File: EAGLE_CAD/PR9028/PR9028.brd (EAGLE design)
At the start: 65.9 x 66 mm, 61 parts, among them SW1 C&K_PTS645, T1 TPTP20R, T10 TPTP20R, T11 TPTP20R, T12 TPTP20R, T13 TPTP20R, T14 TPTP20R, T15 TPTP20R, T16 TPTP20R, T17 TPTP20R, T2 TPTP20R, T4 TPTP20R, T5 TPTP20R, T6 TPTP20R, T7 TPTP20R, T8 TPTP20R, T9 TPTP20R, U1 FMIC

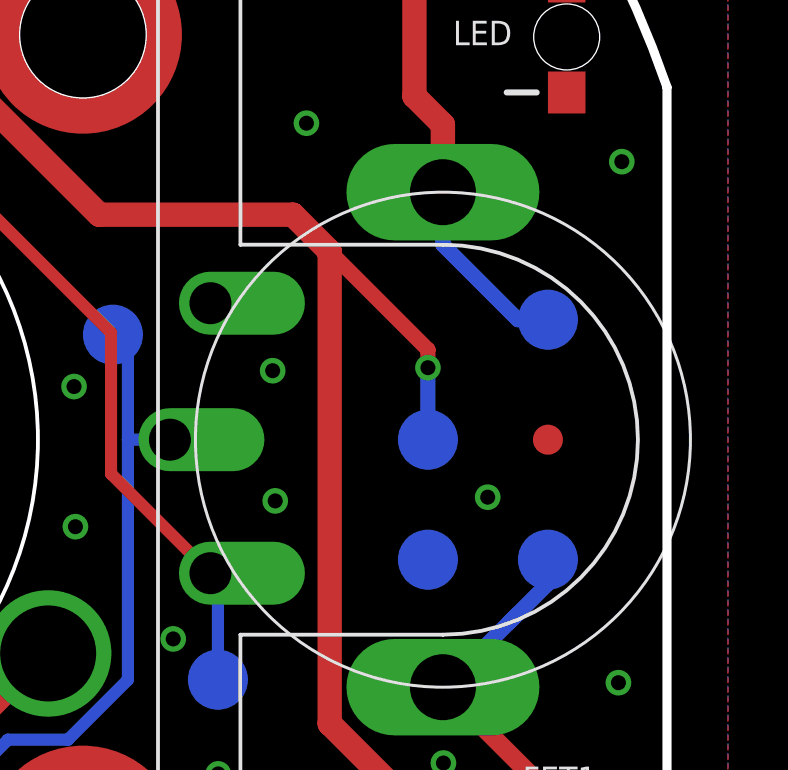
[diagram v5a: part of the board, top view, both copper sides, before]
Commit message: 9028 Updates
Updated test points to match PR9027
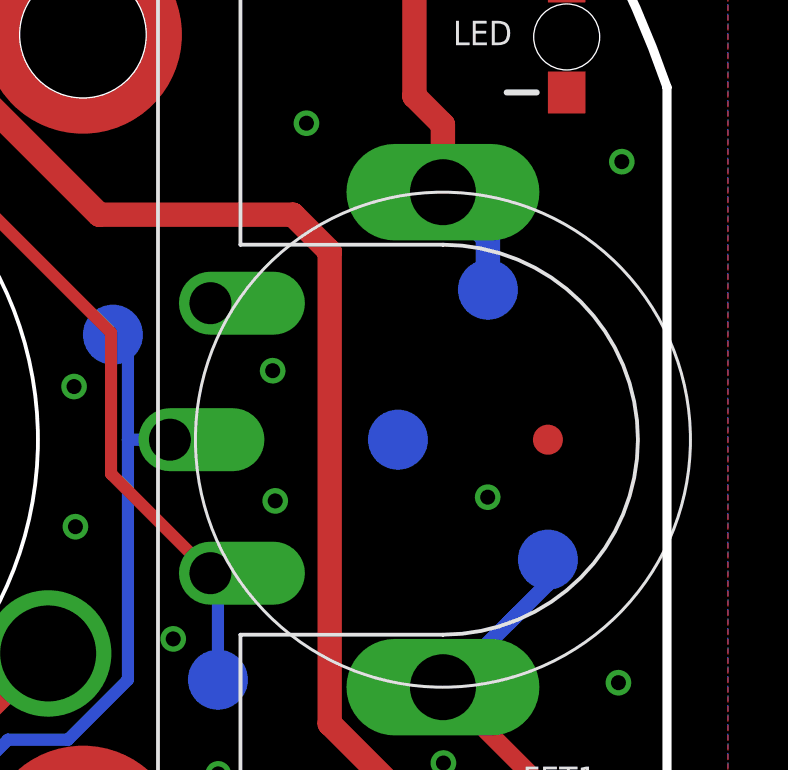
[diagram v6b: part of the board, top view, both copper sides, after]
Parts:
- removed T4: TPTP20R, PR_Parts_Library:TP20R
- moved T2 4.12 mm to (59.0, 35.0)
- moved T15 2.24 mm to (62.0, 40.0)
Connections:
- net VCC: no longer T4.TP
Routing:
- net VCC: track 110.0 -> 102.4 mm, vias 3 -> 2
- net SW_OUT: track 24.2 -> 21.8 mm
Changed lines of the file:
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@@
 <attribute name="VALUE" x="11.362" y="43.584" size="0.0254" layer="28" rot="MR0"/>
 </element>
-<element name="T2" library="PR_Parts_Library" package="TP20R" value="TPTP20R" x="60" y="31" smashed="yes" rot="MR0">
-<attribute name="MFG_PN" value="DNP" x="60" y="31" size="1.778" layer="28" rot="MR0" display="off"/>
-<attribute name="NAME" x="60.3625" y="28.7001" size="0.6096" layer="26" font="vector" ratio="16" rot="MR0"/>
-<attribute name="VALUE" x="60.508" y="30.238" size="0.254" layer="28" rot="MR0"/>
-</element>
-<element name="T4" library="PR_Parts_Library" package="TP20R" value="TPTP20R" x="60" y="35" smashed="yes" rot="MR0">
-<attribute name="MFG_PN" value="DNP" x="60" y="35" size="1.778" layer="28" rot="MR0" display="off"/>
-<attribute name="NAME" x="61.8875" y="33.3376" size="0.6096" layer="26" font="vector" ratio="16" rot="MR0"/>
-<attribute name="VALUE" x="60.508" y="34.238" size="0.254" layer="28" rot="MR0"/>
+<element name="T2" library="PR_Parts_Library" package="TP20R" value="TPTP20R" x="59" y="35" smashed="yes" rot="MR0">
+<attribute name="MFG_PN" value="DNP" x="59" y="35" size="1.778" layer="28" rot="MR0" display="off"/>
+<attribute name="NAME" x="59.3625" y="32.7001" size="0.6096" layer="26" font="vector" ratio="16" rot="MR0"/>
+<attribute name="VALUE" x="59.508" y="34.238" size="0.254" layer="28" rot="MR0"/>
 </element>
 <element name="T5" library="PR_Parts_Library" package="TP20R" value="TPTP20R" x="41" y="65.5" smashed="yes" rot="MR0">
@@
 <attribute name="VALUE" x="64.762" y="29.984" size="0.0254" layer="28" rot="MR0"/>
 </element>
-<element name="T15" library="PR_Parts_Library" package="TP20R" value="TPTP20R" x="64" y="39" smashed="yes" rot="MR0">
-<attribute name="MFG_PN" value="DNP" x="64" y="39" size="1.778" layer="28" rot="MR0" display="off"/>
-<attribute name="NAME" x="65.0625" y="36.925" size="0.6096" layer="26" font="vector" ratio="16" rot="MR0"/>
-<attribute name="VALUE" x="64.762" y="37.984" size="0.0254" layer="28" rot="MR0"/>
+<element name="T15" library="PR_Parts_Library" package="TP20R" value="TPTP20R" x="62" y="40" smashed="yes" rot="MR0">
+<attribute name="MFG_PN" value="DNP" x="62" y="40" size="1.778" layer="28" rot="MR0" display="off"/>
+<attribute name="NAME" x="63.0625" y="37.925" size="0.6096" layer="26" font="vector" ratio="16" rot="MR0"/>
+<attribute name="VALUE" x="62.762" y="38.984" size="0.0254" layer="28" rot="MR0"/>
 </element>
 <element name="T16" library="PR_Parts_Library" package="TP20R" value="TPTP20R" x="53" y="27" smashed="yes" rot="MR0">
@@
 <contactref element="C33" pad="1"/>
 <contactref element="C40" pad="P$1"/>
-<contactref element="T4" pad="TP"/>
 <contactref element="T5" pad="TP"/>
 <contactref element="C32" pad="1"/>
@@
 <wire x1="40.35669375" y1="65.48169375" x2="40.4008875" y2="65.5" width="0.254" layer="16" curve="-45"/>
 <wire x1="40.4008875" y1="65.5" x2="41" y2="65.5" width="0.254" layer="16"/>
-<via x="60" y="37.4" extent="1-16" drill="0.5"/>
 <wire x1="37.54" y1="65.77" x2="39.06" y2="64.25" width="0.254" layer="16"/>
 <wire x1="39.06" y1="64.25" x2="39.125" y2="64.25" width="0.254" layer="16"/>
@@
 <wire x1="59.6" y1="21.2" x2="60.25" y2="20.55" width="0.8128" layer="1"/>
 <wire x1="60.25" y1="20.55" x2="61.8" y2="20.55" width="0.8128" layer="1"/>
-<wire x1="60" y1="35" x2="60" y2="37.4" width="0.508" layer="16"/>
-<wire x1="56.7252" y1="41.2748" x2="60" y2="38" width="0.508" layer="1"/>
-<wire x1="60" y1="38" x2="60" y2="37.4" width="0.508" layer="1"/>
 <wire x1="37.2" y1="53.9508875" x2="37.6508875" y2="53.5" width="0.4064" layer="16"/>
 <wire x1="37.2" y1="58.8" x2="36.6" y2="59.4" width="0.4064" layer="16"/>
@@
 <wire x1="59.55" y1="53.5" x2="59.55" y2="46.45" width="0.8128" layer="1"/>
 <wire x1="59.55" y1="46.45" x2="60.5" y2="45.5" width="0.8128" layer="1"/>
-<wire x1="63" y1="39" x2="60.5" y2="41.5" width="0.508" layer="16"/>
-<wire x1="63" y1="39" x2="64" y2="39" width="0.508" layer="16"/>
-<wire x1="60.5" y1="41.5" x2="60.5" y2="43.25" width="0.508" layer="16"/>
+<wire x1="60.5" y1="43.25" x2="62" y2="41.75" width="0.8128" layer="16"/>
+<wire x1="62" y1="41.75" x2="62" y2="40" width="0.8128" layer="16"/>
 </signal>
 <signal name="ANT" class="1">

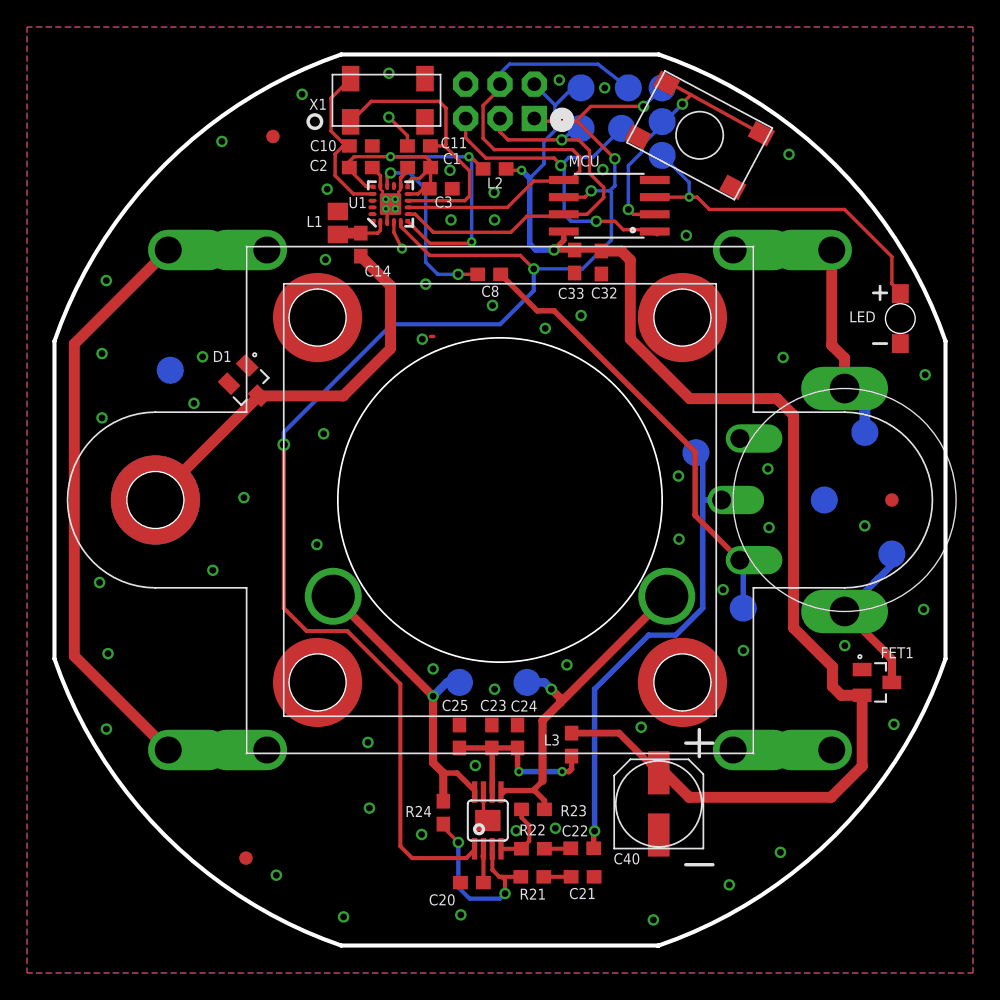
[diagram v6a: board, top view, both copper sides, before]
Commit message: changed batteries, few other small things
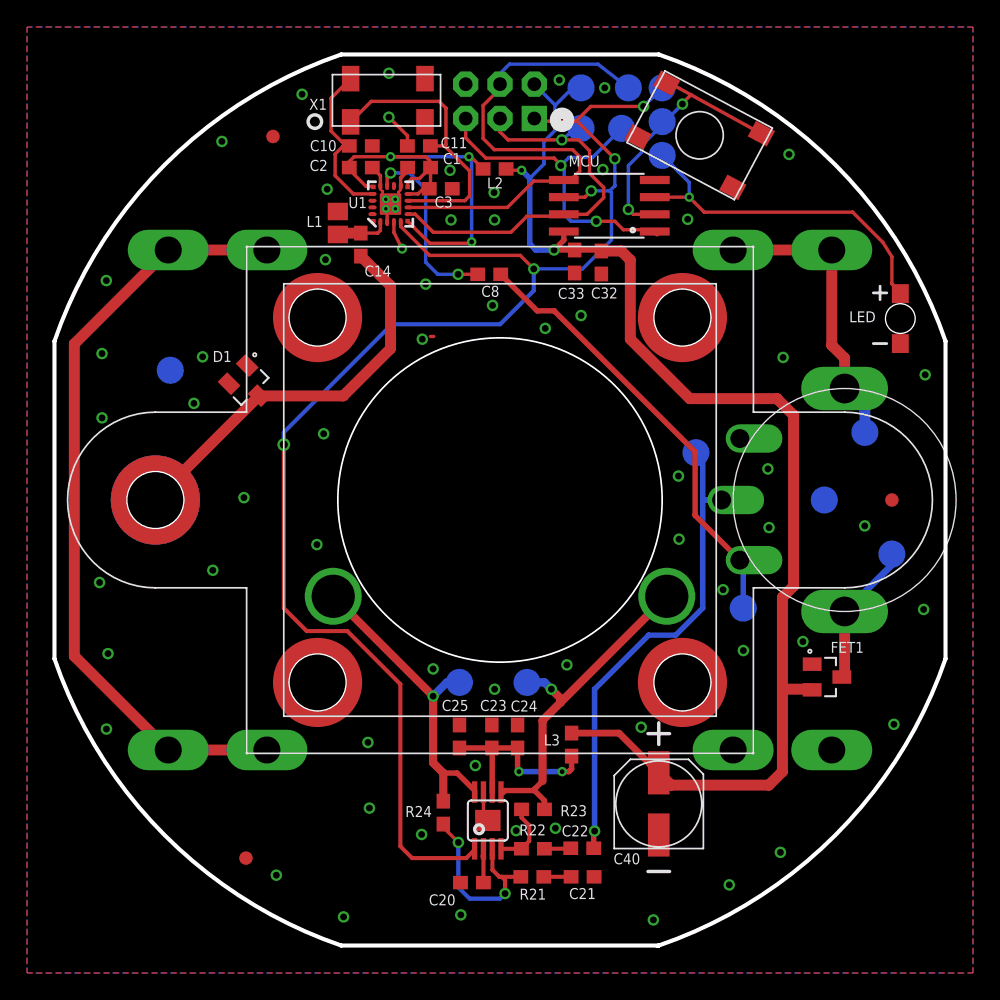
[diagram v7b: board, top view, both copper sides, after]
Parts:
- moved FET1 3.72 mm to (59.2, 21.9)
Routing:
- net VCC: track 102.4 -> 95.4 mm
- net SW_IN: track 12.8 -> 10.7 mm
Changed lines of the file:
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@@
 <?xml version="1.0" encoding="utf-8"?>
 <!DOCTYPE eagle SYSTEM "eagle.dtd">
-<eagle version="8.4.3">
+<eagle version="8.5.0">
 <drawing>
 <settings>
@@
 <param name="checkRestrict" value="1"/>
 <param name="checkStop" value="0"/>
+<param name="checkValues" value="0"/>
 <param name="useDiameter" value="13"/>
 <param name="maxErrors" value="50"/>
@@
 <attribute name="MFG_PN" value="Consigned" x="35" y="53.5" size="1.778" layer="28" rot="MR180" display="off"/>
 </element>
-<element name="JP6" library="PR_Parts_Library" package="BK92_AA_BATT" value="BK-92_MPD_AA_BATT_CLIP" x="35" y="16.5" locked="yes" rot="MR0">
+<element name="JP6" library="PR_Parts_Library" package="BK92_AA_BATT" value="BK-92_MPD_AA_BATT_CLIP" x="35" y="16.5" rot="MR0">
 <attribute name="CENTERLINE_PN" value="PR2003" x="35" y="16.5" size="1.778" layer="28" rot="MR0" display="off"/>
 <attribute name="MFG_PN" value="Consigned" x="35" y="16.5" size="1.778" layer="28" rot="MR0" display="off"/>
@@
 <attribute name="VOLTAGE" value="10V" x="34.2" y="51.7" size="1.778" layer="27" display="off"/>
 </element>
-<element name="FET1" library="PR_Parts_Library" package="SOT23_CPL" value="" x="62.9" y="21.5" smashed="yes">
-<attribute name="ALTERNATE_MFG_PN" value="AO3415A" x="62.9" y="21.5" size="1.778" layer="27" display="off"/>
-<attribute name="MFG_PN" value="AO3435" x="62.9" y="21.5" size="1.778" layer="27" display="off"/>
-<attribute name="NAME" x="65.6245" y="24.103" size="0.8128" layer="25" font="vector" ratio="18" rot="R180"/>
-<attribute name="VALUE" x="61.884" y="21.3095" size="0.4064" layer="27"/>
+<element name="FET1" library="PR_Parts_Library" package="SOT23_CPL" value="" x="59.2" y="21.9" smashed="yes">
+<attribute name="ALTERNATE_MFG_PN" value="AO3415A" x="59.2" y="21.9" size="1.778" layer="27" display="off"/>
+<attribute name="MFG_PN" value="AO3435" x="59.2" y="21.9" size="1.778" layer="27" display="off"/>
+<attribute name="NAME" x="61.9245" y="24.503" size="0.8128" layer="25" font="vector" ratio="18" rot="R180"/>
+<attribute name="VALUE" x="58.184" y="21.7095" size="0.4064" layer="27"/>
 </element>
 <element name="SPEAKER" library="PR_Parts_Library" package="PR2023_GROUND_UP_SPEAKER" value="PR2023_GROUND_UP_SPEAKER" x="35" y="35" locked="yes">
@@
 <via x="25.3375" y="12.2" extent="1-16" drill="0.5"/>
 <via x="66.4625" y="44.2675" extent="1-16" drill="0.5"/>
-<via x="60.51625" y="24.2225" extent="1-16" drill="0.5"/>
+<via x="57.41625" y="24.5225" extent="1-16" drill="0.5"/>
 <via x="51.96625" y="6.5175" extent="1-16" drill="0.5"/>
 <wire x1="33.775" y1="13.38625" x2="33.775" y2="11.61125" width="0.254" layer="1"/>
@@
 <wire x1="28.15" y1="61.9575" x2="26.77875" y2="63.32875" width="0.254" layer="1"/>
 <via x="66.35" y="26.9" extent="1-16" drill="0.5"/>
-<via x="48.7875" y="54.575" extent="1-16" drill="0.5"/>
+<via x="48.8875" y="55.775" extent="1-16" drill="0.5"/>
 <wire x1="26.65" y1="55.565" x2="26.65" y2="56.45" width="0.254" layer="1"/>
 <wire x1="26.65" y1="56.45" x2="26.55" y2="56.55" width="0.254" layer="1"/>
@@
 <wire x1="39.06" y1="62.335" x2="39.06" y2="64.25" width="0.254" layer="16"/>
 <wire x1="42.5" y1="53.425" x2="43.975" y2="53.425" width="0.8128" layer="1"/>
-<wire x1="61.8" y1="20.55" x2="61.8" y2="15.3" width="0.8128" layer="1"/>
-<wire x1="55.5" y1="42.5" x2="56.7252" y2="41.2748" width="0.8128" layer="1"/>
-<wire x1="56.7252" y1="41.2748" x2="56.7252" y2="25.5345375" width="0.8128" layer="1"/>
-<wire x1="44.6412" y1="52.7588" x2="44.6412" y2="46.90163125" width="0.8128" layer="1"/>
+<wire x1="56.7252" y1="41.2748" x2="55.5" y2="42.5" width="0.8128" layer="1"/>
+<wire x1="44.6412" y1="46.90163125" x2="44.6412" y2="52.7588" width="0.8128" layer="1"/>
 <wire x1="44.6412" y1="46.90163125" x2="49.04283125" y2="42.5" width="0.8128" layer="1"/>
 <wire x1="49.04283125" y1="42.5" x2="55.5" y2="42.5" width="0.8128" layer="1"/>
 <wire x1="43.975" y1="53.425" x2="44.6412" y2="52.7588" width="0.8128" layer="1"/>
-<wire x1="61.7097375" y1="20.55" x2="61.8" y2="20.55" width="0.8128" layer="1"/>
-<wire x1="47.19" y1="14.81" x2="46.75" y2="14.81" width="0.8128" layer="1"/>
-<wire x1="47.19" y1="14.81" x2="49" y2="13" width="0.8128" layer="1"/>
-<wire x1="49" y1="13" x2="59.5" y2="13" width="0.8128" layer="1"/>
-<wire x1="59.5" y1="13" x2="61.8" y2="15.3" width="0.8128" layer="1"/>
 <contactref element="L3" pad="1"/>
 <wire x1="46.75" y1="14.81" x2="46.06" y2="15.5" width="0.508" layer="1"/>
@@
 <wire x1="43.81" y1="17.75" x2="40.3" y2="17.75" width="0.508" layer="1"/>
 <wire x1="46.75" y1="14.81" x2="43.81" y2="17.75" width="0.508" layer="1"/>
-<wire x1="56.7252" y1="25.5345375" x2="59.6" y2="22.6597375" width="0.8128" layer="1"/>
-<wire x1="59.6" y1="22.6597375" x2="59.6" y2="21.2" width="0.8128" layer="1"/>
-<wire x1="59.6" y1="21.2" x2="60.25" y2="20.55" width="0.8128" layer="1"/>
-<wire x1="60.25" y1="20.55" x2="61.8" y2="20.55" width="0.8128" layer="1"/>
 <wire x1="37.2" y1="53.9508875" x2="37.6508875" y2="53.5" width="0.4064" layer="16"/>
 <wire x1="37.2" y1="58.8" x2="36.6" y2="59.4" width="0.4064" layer="16"/>
@@
 <wire x1="38.25" y1="60.0258875" x2="38.25" y2="59.85" width="0.254" layer="16"/>
 <wire x1="38.25" y1="59.85" x2="37.2" y2="58.8" width="0.254" layer="16"/>
+<wire x1="56.7252" y1="41.2748" x2="56.7252" y2="28.6252" width="0.8128" layer="1"/>
+<wire x1="55.9" y1="14.9" x2="54.9" y2="13.9" width="0.8128" layer="1"/>
+<wire x1="56.7252" y1="28.6252" x2="55.9" y2="27.8" width="0.8128" layer="1"/>
+<wire x1="55.9" y1="27.8" x2="55.9" y2="21" width="0.8128" layer="1"/>
+<wire x1="55.9" y1="21" x2="55.9" y2="14.9" width="0.8128" layer="1"/>
+<wire x1="54.9" y1="13.9" x2="47.66" y2="13.9" width="0.8128" layer="1"/>
+<wire x1="47.66" y1="13.9" x2="46.75" y2="14.81" width="0.8128" layer="1"/>
+<wire x1="58.1" y1="20.95" x2="58.05" y2="21" width="0.8128" layer="1"/>
+<wire x1="58.05" y1="21" x2="55.9" y2="21" width="0.8128" layer="1"/>
 </signal>
 <signal name="A_OUT">
@@
 <contactref element="FET1" pad="3"/>
 <contactref element="T14" pad="TP"/>
-<wire x1="63.5" y1="23.7241125" x2="63.48169375" y2="23.76830625" width="0.6096" layer="1" curve="45"/>
-<wire x1="63.48169375" y1="23.76830625" x2="60.5" y2="26.75" width="0.6096" layer="1"/>
-<wire x1="64" y1="21.5" x2="64" y2="23.198225" width="0.6096" layer="1"/>
-<wire x1="64" y1="23.198225" x2="63.98169375" y2="23.24241875" width="0.6096" layer="1" curve="45"/>
-<wire x1="63.98169375" y1="23.24241875" x2="63.5" y2="23.7241125" width="0.6096" layer="1"/>
 <wire x1="64" y1="31" x2="64" y2="30.2" width="0.508" layer="16"/>
-<wire x1="64" y1="30.2" x2="63" y2="29.2" width="0.508" layer="16"/>
-<wire x1="63" y1="29.2" x2="62.7" y2="28.9" width="0.508" layer="16"/>
-<wire x1="63" y1="29.2" x2="60.55" y2="26.75" width="0.508" layer="16"/>
+<wire x1="64" y1="30.2" x2="60.55" y2="26.75" width="0.508" layer="16"/>
 <wire x1="60.55" y1="26.75" x2="60.5" y2="26.75" width="0.508" layer="16"/>
+<wire x1="60.5" y1="26.75" x2="60.5" y2="22.1" width="0.8128" layer="1"/>
+<wire x1="60.5" y1="22.1" x2="60.3" y2="21.9" width="0.8128" layer="1"/>
 </signal>
 <signal name="A_IN">
@@
 <contactref element="LED" pad="P$1"/>
 <wire x1="47.4008875" y1="60.125" x2="47.35669375" y2="60.14330625" width="0.254" layer="16" curve="-45"/>
-<wire x1="64" y1="51" x2="64" y2="53" width="0.254" layer="1"/>
+<wire x1="64" y1="53" x2="64" y2="51" width="0.254" layer="1"/>
 <wire x1="64" y1="51" x2="64.625" y2="50.375" width="0.254" layer="1"/>
 <wire x1="64.625" y1="50.375" x2="64.625" y2="50.275" width="0.254" layer="1"/>
-<wire x1="60.5" y1="56.5" x2="50.5" y2="56.5" width="0.254" layer="1"/>
-<wire x1="64" y1="53" x2="60.5" y2="56.5" width="0.254" layer="1"/>
 <wire x1="46.5432" y1="57.5" x2="46.4532" y2="57.41" width="0.254" layer="1"/>
-<wire x1="50.5" y1="56.5" x2="49.59" y2="57.41" width="0.254" layer="1"/>
-<wire x1="49.59" y1="57.41" x2="49" y2="57.41" width="0.254" layer="1"/>
 <wire x1="49" y1="57.41" x2="46.4532" y2="57.41" width="0.254" layer="1"/>
 <wire x1="49" y1="58.5" x2="47" y2="60.5" width="0.254" layer="16"/>
@@
 <wire x1="47" y1="60.5" x2="47.375" y2="60.125" width="0.254" layer="16"/>
 <wire x1="47.375" y1="60.125" x2="47.4008875" y2="60.125" width="0.254" layer="16"/>
+<wire x1="64" y1="53" x2="63.333696875" y2="54.066303125" width="0.254" layer="1"/>
+<wire x1="50.11" y1="56.3" x2="49" y2="57.41" width="0.254" layer="1"/>
+<wire x1="63.333696875" y1="54.066303125" x2="61.1" y2="56.3" width="0.254" layer="1"/>
+<wire x1="61.1" y1="56.3" x2="50.11" y2="56.3" width="0.254" layer="1"/>
 </signal>
 <signal name="N$13">

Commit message: PR9028_Rev_B
Minor DFM Updates
- moved c40
- moved c14
- increased solder mask
- moved vcc trace away from NE speaker pem nut
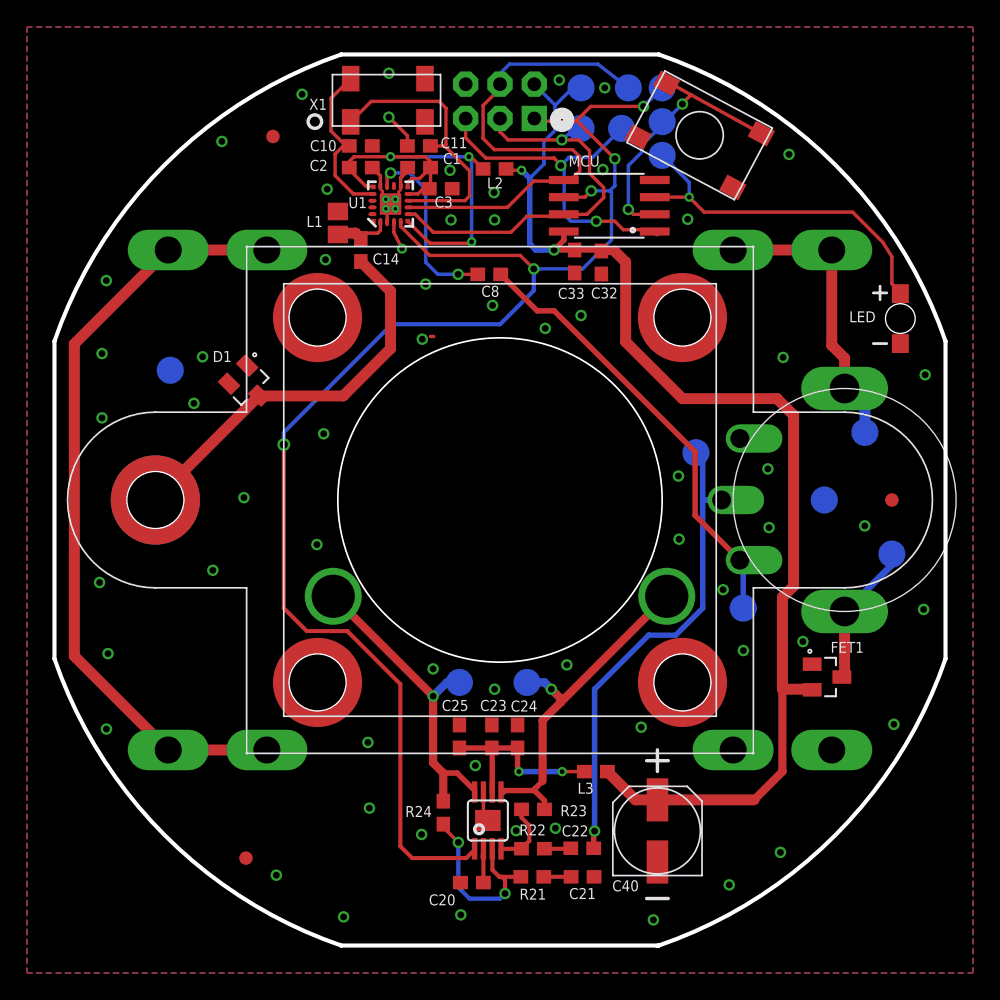
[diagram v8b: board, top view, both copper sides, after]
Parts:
- moved L3 2.69 mm to (42.1, 14.9), turned to 180 degrees
- moved C40 2.00 mm to (46.6, 10.5)
- moved C14 0.40 mm to (24.7, 53.5)
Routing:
- net VCC: track 95.4 -> 91.5 mm
- net ANT: track 30.0 -> 29.4 mm
